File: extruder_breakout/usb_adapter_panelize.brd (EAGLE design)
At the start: 38.1 x 22.9 mm, 6 parts, among them X1 9090-4V, X2 PN87520-S, X3 22-23-2031, X4 22-23-2031

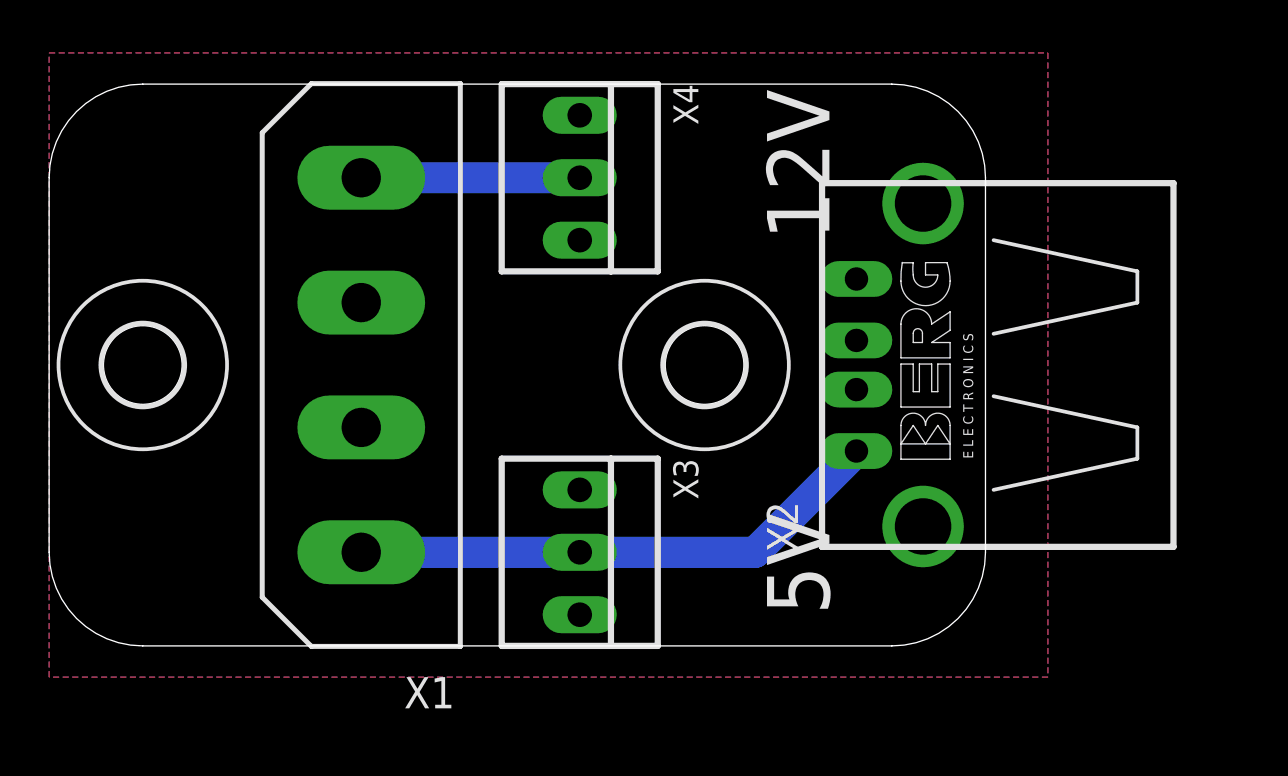
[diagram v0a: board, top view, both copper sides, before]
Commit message: behebt kleine Fehler im Stromverteiler-Board
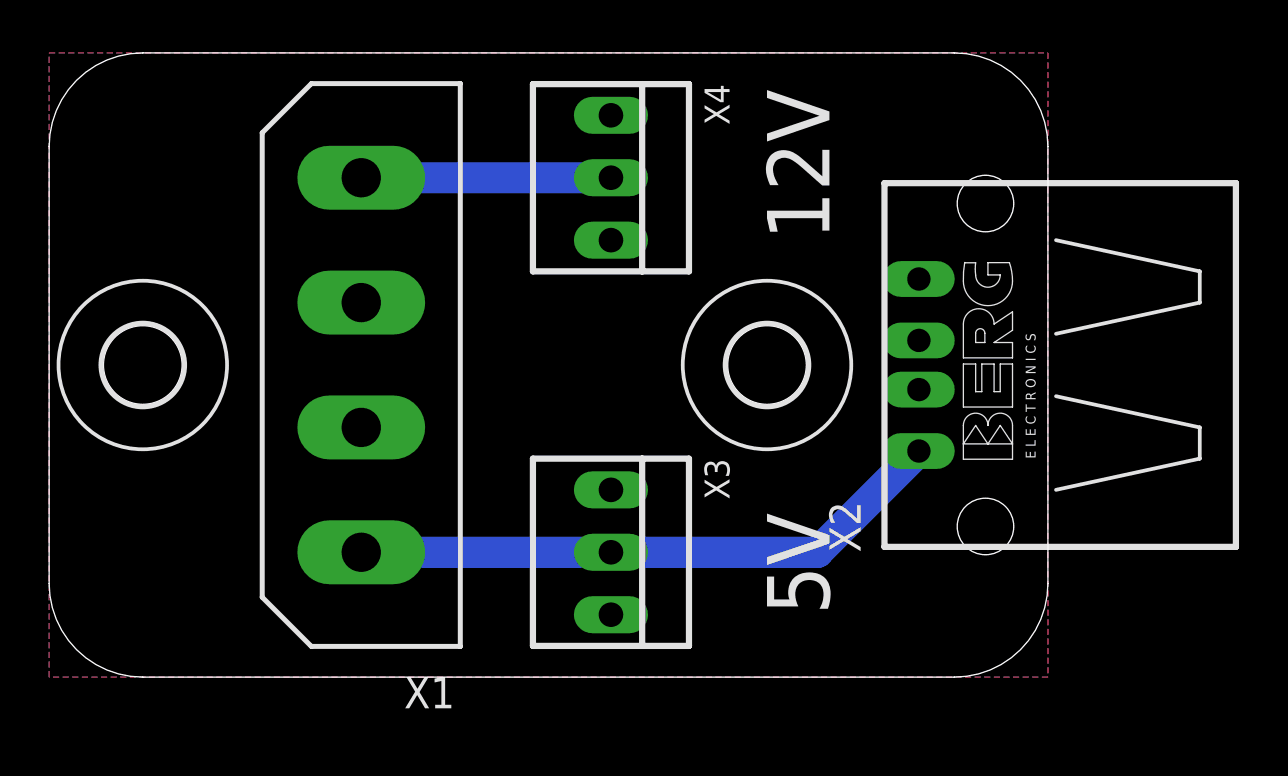
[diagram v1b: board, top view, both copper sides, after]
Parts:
- X2: value PN87520-S -> (none); device con-berg:PN87520-S -> con-berg:PN87520
- moved H2 2.54 mm to (29.2, 12.7)
- moved X2 2.54 mm to (38.1, 12.7)
- moved X3 1.27 mm to (22.9, 5.08)
- moved X4 1.27 mm to (22.9, 20.3)
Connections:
- net GND: now also X3.1, X4.1; no longer X2.S1, X2.S2, X3.3, X4.3
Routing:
- net +5V: track 21.9 -> 24.4 mm
- net +12V: track 8.89 -> 10.2 mm
- added copper zone on layer 1, net N$1
- removed copper zone on layer 1, net GND
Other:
- board size 38.1 x 22.9 mm -> 40.6 x 25.4 mm
- board text added: "X1"
- board text added: "X2"
- board text added: "X3"
- board text added: "X4"
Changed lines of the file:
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@@
 <layer number="97" name="Info" color="7" fill="1" visible="no" active="no"/>
 <layer number="98" name="Guide" color="6" fill="1" visible="no" active="no"/>
+<layer number="125" name="_tNames" color="14" fill="1" visible="yes" active="yes"/>
 </layers>
 <board>
@@
 <text x="31.75" y="17.78" size="2.54" layer="25" font="vector" rot="R90">12V</text>
 <text x="31.75" y="2.54" size="2.54" layer="25" font="vector" rot="R90">5V</text>
-<wire x1="0" y1="20.32" x2="0" y2="5.08" width="0" layer="20"/>
-<wire x1="0" y1="5.08" x2="3.81" y2="1.27" width="0" layer="20" curve="90"/>
-<wire x1="3.81" y1="1.27" x2="34.29" y2="1.27" width="0" layer="20"/>
-<wire x1="34.29" y1="1.27" x2="38.1" y2="5.08" width="0" layer="20" curve="90"/>
-<wire x1="38.1" y1="5.08" x2="38.1" y2="20.32" width="0" layer="20"/>
-<wire x1="38.1" y1="20.32" x2="34.29" y2="24.13" width="0" layer="20" curve="90"/>
-<wire x1="34.29" y1="24.13" x2="3.81" y2="24.13" width="0" layer="20"/>
-<wire x1="3.81" y1="24.13" x2="0" y2="20.32" width="0" layer="20" curve="90"/>
+<wire x1="0" y1="21.59" x2="0" y2="3.81" width="0" layer="20"/>
+<wire x1="0" y1="3.81" x2="3.81" y2="0" width="0" layer="20" curve="90"/>
+<wire x1="3.81" y1="0" x2="36.83" y2="0" width="0" layer="20"/>
+<wire x1="36.83" y1="0" x2="40.64" y2="3.81" width="0" layer="20" curve="90"/>
+<wire x1="40.64" y1="3.81" x2="40.64" y2="21.59" width="0" layer="20"/>
+<wire x1="40.64" y1="21.59" x2="36.83" y2="25.4" width="0" layer="20" curve="90"/>
+<wire x1="36.83" y1="25.4" x2="3.81" y2="25.4" width="0" layer="20"/>
+<wire x1="3.81" y1="25.4" x2="0" y2="21.59" width="0" layer="20" curve="90"/>
+<text x="7.62" y="3.81" size="1.27" layer="125" rot="R180">X1</text>
+<text x="33.02" y="5.08" size="1.27" layer="125" rot="R90">X2</text>
+<text x="26.67" y="8.89" size="1.016" layer="125" ratio="10" rot="R270">X3</text>
+<text x="26.67" y="24.13" size="1.016" layer="125" ratio="10" rot="R270">X4</text>
 </plain>
 <attributes>
@@
 <attribute name="OC_FARNELL" value="unknown" x="35.56" y="38.1" size="1.778" layer="27" rot="R90" display="off"/>
 </element>
-<element name="X2" library="con-berg" package="PN87520-S" value="PN87520-S" x="35.56" y="12.7" rot="R90">
-<attribute name="OC_NEWARK" value="unknown" x="46.99" y="34.29" size="1.778" layer="27" rot="R90" display="off"/>
-<attribute name="MPN" value="" x="46.99" y="34.29" size="1.778" layer="27" rot="R90" display="off"/>
-<attribute name="MF" value="" x="46.99" y="34.29" size="1.778" layer="27" rot="R90" display="off"/>
-<attribute name="OC_FARNELL" value="unknown" x="46.99" y="34.29" size="1.778" layer="27" rot="R90" display="off"/>
-</element>
-<element name="X3" library="con-molex" package="22-23-2031" value="22-23-2031" x="21.59" y="5.08" rot="R270">
-<attribute name="OC_NEWARK" value="30C0862" x="-13.97" y="-12.7" size="1.778" layer="27" rot="R270" display="off"/>
-<attribute name="MPN" value="22-23-2031" x="-13.97" y="-12.7" size="1.778" layer="27" rot="R270" display="off"/>
-<attribute name="MF" value="MOLEX" x="-13.97" y="-12.7" size="1.778" layer="27" rot="R270" display="off"/>
-<attribute name="OC_FARNELL" value="1462950" x="-13.97" y="-12.7" size="1.778" layer="27" rot="R270" display="off"/>
-</element>
-<element name="X4" library="con-molex" package="22-23-2031" value="22-23-2031" x="21.59" y="20.32" rot="R270">
-<attribute name="OC_NEWARK" value="30C0862" x="-13.97" y="-6.35" size="1.778" layer="27" rot="R270" display="off"/>
-<attribute name="MPN" value="22-23-2031" x="-13.97" y="-6.35" size="1.778" layer="27" rot="R270" display="off"/>
-<attribute name="MF" value="MOLEX" x="-13.97" y="-6.35" size="1.778" layer="27" rot="R270" display="off"/>
-<attribute name="OC_FARNELL" value="1462950" x="-13.97" y="-6.35" size="1.778" layer="27" rot="R270" display="off"/>
+<element name="X2" library="con-berg" package="PN87520" value="" x="38.1" y="12.7" rot="R90">
+<attribute name="OC_NEWARK" value="unknown" x="49.53" y="34.29" size="1.778" layer="27" rot="R90" display="off"/>
+<attribute name="MPN" value="" x="49.53" y="34.29" size="1.778" layer="27" rot="R90" display="off"/>
+<attribute name="MF" value="" x="49.53" y="34.29" size="1.778" layer="27" rot="R90" display="off"/>
+<attribute name="OC_FARNELL" value="unknown" x="49.53" y="34.29" size="1.778" layer="27" rot="R90" display="off"/>
+</element>
+<element name="X3" library="con-molex" package="22-23-2031" value="22-23-2031" x="22.86" y="5.08" rot="R270">
+<attribute name="OC_NEWARK" value="30C0862" x="-12.7" y="-12.7" size="1.778" layer="27" rot="R270" display="off"/>
+<attribute name="MPN" value="22-23-2031" x="-12.7" y="-12.7" size="1.778" layer="27" rot="R270" display="off"/>
+<attribute name="MF" value="MOLEX" x="-12.7" y="-12.7" size="1.778" layer="27" rot="R270" display="off"/>
+<attribute name="OC_FARNELL" value="1462950" x="-12.7" y="-12.7" size="1.778" layer="27" rot="R270" display="off"/>
+</element>
+<element name="X4" library="con-molex" package="22-23-2031" value="22-23-2031" x="22.86" y="20.32" rot="R270">
+<attribute name="OC_NEWARK" value="30C0862" x="-12.7" y="-6.35" size="1.778" layer="27" rot="R270" display="off"/>
+<attribute name="MPN" value="22-23-2031" x="-12.7" y="-6.35" size="1.778" layer="27" rot="R270" display="off"/>
+<attribute name="MF" value="MOLEX" x="-12.7" y="-6.35" size="1.778" layer="27" rot="R270" display="off"/>
+<attribute name="OC_FARNELL" value="1462950" x="-12.7" y="-6.35" size="1.778" layer="27" rot="R270" display="off"/>
 </element>
 <element name="H1" library="holes" package="3,2" value="MOUNT-HOLE3.2" x="3.81" y="12.7"/>
-<element name="H2" library="holes" package="3,2" value="MOUNT-HOLE3.2" x="26.67" y="12.7"/>
+<element name="H2" library="holes" package="3,2" value="MOUNT-HOLE3.2" x="29.21" y="12.7"/>
 </elements>
 <signals>
 <signal name="GND">
+<contactref element="X4" pad="1"/>
+<contactref element="X3" pad="1"/>
 <contactref element="X1" pad="3"/>
 <contactref element="X1" pad="2"/>
@@
 <vertex x="0" y="0"/>
 </polygon>
-<contactref element="X4" pad="3"/>
-<contactref element="X3" pad="3"/>
-<contactref element="X2" pad="S2"/>
-<contactref element="X2" pad="S1"/>
+</signal>
+<signal name="+12V">
+<contactref element="X4" pad="2"/>
+<contactref element="X1" pad="4"/>
+<wire x1="12.7" y1="20.32" x2="22.86" y2="20.32" width="1.27" layer="16"/>
+</signal>
+<signal name="+5V">
+<contactref element="X3" pad="2"/>
+<contactref element="X2" pad="1"/>
+<contactref element="X1" pad="1"/>
+<wire x1="12.7" y1="5.08" x2="22.86" y2="5.08" width="1.27" layer="16"/>
+<wire x1="35.39" y1="9.2" x2="31.27" y2="5.08" width="1.27" layer="16"/>
+<wire x1="31.27" y1="5.08" x2="22.86" y2="5.08" width="1.27" layer="16"/>
+</signal>
+<signal name="N$1">
 <polygon width="0.4064" layer="1">
 <vertex x="0" y="25.4"/>
@@
 </polygon>
 </signal>
-<signal name="+12V">
-<contactref element="X4" pad="2"/>
-<contactref element="X1" pad="4"/>
-<wire x1="12.7" y1="20.32" x2="21.59" y2="20.32" width="1.27" layer="16"/>
-</signal>
-<signal name="+5V">
-<contactref element="X3" pad="2"/>
-<contactref element="X2" pad="1"/>
-<contactref element="X1" pad="1"/>
-<wire x1="12.7" y1="5.08" x2="21.59" y2="5.08" width="1.27" layer="16"/>
-<wire x1="32.85" y1="9.2" x2="28.73" y2="5.08" width="1.27" layer="16"/>
-<wire x1="28.73" y1="5.08" x2="21.59" y2="5.08" width="1.27" layer="16"/>
-</signal>
 </signals>
